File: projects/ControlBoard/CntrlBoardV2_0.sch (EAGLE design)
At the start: 106 parts

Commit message: Updated with processor test board V2
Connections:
- removed net PA12: SAMD21J.PA12
- net PA07: no longer C17.1, CH1-DM.A, CH2-DM.A, PH_AMP_2.OUT, R14.1, R34.2, TD-DM.1A
- net PB00: now also C17.1, CH1-DM.A, CH2-DM.A, PH_AMP_2.OUT, R14.1, R34.2, TD-DM.1A
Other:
- note added: "CONTAINS ERRORS IN PINNOUT DO NOT COPY"
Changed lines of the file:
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@@
 <?xml version="1.0" encoding="utf-8"?>
 <!DOCTYPE eagle SYSTEM "eagle.dtd">
-<eagle version="7.3.0">
+<eagle version="7.6.0">
 <drawing>
 <settings>
@@
 <text x="154.94" y="12.7" size="1.778" layer="95">Radio</text>
 <text x="152.4" y="86.36" size="1.778" layer="95">Solar Panels</text>
-<text x="152.4" y="96.52" size="1.778" layer="95">Sensors</text>
 <text x="152.4" y="104.14" size="1.778" layer="95">I2C</text>
 <text x="152.4" y="101.6" size="1.778" layer="95">I2C</text>
@@
 <text x="63.5" y="66.04" size="1.778" layer="95">NC</text>
 <text x="50.8" y="55.88" size="1.778" layer="97">RD_EN</text>
+<text x="187.96" y="91.44" size="1.778" layer="97">CONTAINS ERRORS IN PINNOUT DO NOT COPY</text>
 </plain>
 <instances>
@@
 </segment>
 </net>
-<net name="PA12" class="0">
-<segment>
-<pinref part="SAMD21J" gate="G$1" pin="PA12"/>
-<wire x1="149.86" y1="96.52" x2="139.7" y2="96.52" width="0.1524" layer="91"/>
-<label x="144.78" y="96.52" size="1.778" layer="95"/>
-</segment>
-</net>
 <net name="PA24" class="0">
 <segment>
@@
 </segment>
 </net>
-<net name="PA07" class="0">
+<net name="LFE_1_MP_NFLT" class="0">
+<segment>
+<pinref part="CH1-DM" gate="G$1" pin="B4"/>
+<wire x1="78.74" y1="88.9" x2="66.04" y2="88.9" width="0.1524" layer="91"/>
+<label x="58.42" y="88.9" size="1.778" layer="95"/>
+</segment>
+</net>
+<net name="VIN" class="0">
+<segment>
+<pinref part="CH2-DM" gate="G$1" pin="B5"/>
+<wire x1="180.34" y1="86.36" x2="193.04" y2="86.36" width="0.1524" layer="91"/>
+<label x="185.42" y="86.36" size="1.778" layer="95"/>
+</segment>
+</net>
+<net name="PB00" class="0">
 <segment>
 <pinref part="R14" gate="G$1" pin="1"/>
@@
 </segment>
 </net>
-<net name="LFE_1_MP_NFLT" class="0">
-<segment>
-<pinref part="CH1-DM" gate="G$1" pin="B4"/>
-<wire x1="78.74" y1="88.9" x2="66.04" y2="88.9" width="0.1524" layer="91"/>
-<label x="58.42" y="88.9" size="1.778" layer="95"/>
-</segment>
-</net>
-<net name="VIN" class="0">
-<segment>
-<pinref part="CH2-DM" gate="G$1" pin="B5"/>
-<wire x1="180.34" y1="86.36" x2="193.04" y2="86.36" width="0.1524" layer="91"/>
-<label x="185.42" y="86.36" size="1.778" layer="95"/>
-</segment>
-</net>

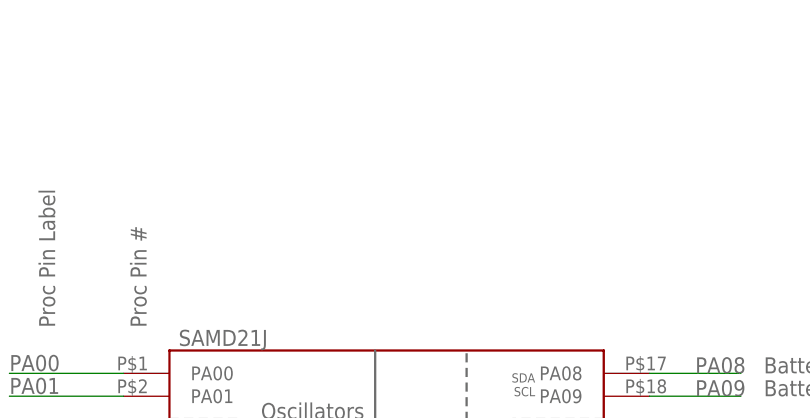
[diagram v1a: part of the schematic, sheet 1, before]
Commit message: LiFePO4 Balancing added
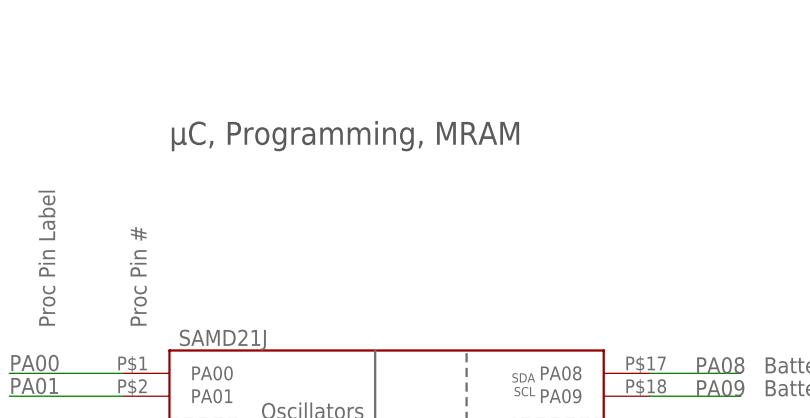
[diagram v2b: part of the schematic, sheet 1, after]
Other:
- note added: "Battery Board Buffers and Connector"
- note added: "Driver Board Connector"
- note added: "Radio Buffers, LEDs, and Connector"
- note added: "Signal Multiplexing"
- note added: "Solar Panel Connectors"
- note added: "Umbilical Connector"
- note added: "µC, Programming, MRAM"
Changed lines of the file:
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@@
 <?xml version="1.0" encoding="utf-8"?>
 <!DOCTYPE eagle SYSTEM "eagle.dtd">
-<eagle version="7.6.0">
+<eagle version="7.7.0">
 <drawing>
 <settings>
@@
 <text x="50.8" y="55.88" size="1.778" layer="97">RD_EN</text>
 <text x="187.96" y="91.44" size="1.778" layer="97">CONTAINS ERRORS IN PINNOUT DO NOT COPY</text>
+<text x="86.36" y="137.16" size="2.54" layer="97">µC, Programming, MRAM</text>
 </plain>
 <instances>
@@
 <plain>
 <text x="-2.54" y="119.38" size="1.27" layer="97">Note (PWM/SYNC) must have voltage greater than 1.5V to ensure PWM mode.</text>
+<text x="40.64" y="127" size="2.54" layer="97">Power Regulation</text>
 </plain>
 <instances>
@@
 <description>Sensors</description>
 <plain>
+<text x="30.48" y="71.12" size="2.54" layer="97">Sensors</text>
 </plain>
 <instances>
@@
 PB03 Return Enable
 PA25 Return In</text>
+<text x="-60.96" y="78.74" size="2.54" layer="97">Radio Buffers, LEDs, and Connector</text>
 </plain>
 <instances>
@@
 <description>Batteries</description>
 <plain>
+<text x="25.4" y="86.36" size="2.54" layer="97">Battery Board Buffers and Connector</text>
 </plain>
 <instances>
@@
 <plain>
 <text x="109.22" y="78.74" size="1.778" layer="97">IR_PMOS</text>
+<text x="35.56" y="101.6" size="2.54" layer="97">Solar Panel Connectors</text>
 </plain>
 <instances>
@@
 <wire x1="-17.78" y1="-15.24" x2="-17.78" y2="38.1" width="0.1524" layer="97" style="shortdash"/>
 <text x="-10.16" y="35.56" size="1.778" layer="97">Photodiode Conversion Circuit</text>
+<text x="-66.04" y="124.46" size="2.54" layer="97">Signal Multiplexing</text>
 </plain>
 <instances>
@@
 <text x="30.48" y="25.4" size="1.778" layer="97" rot="R270">Test Connection</text>
 <text x="121.92" y="76.2" size="1.778" layer="97">LED SHDN_N</text>
+<text x="12.7" y="96.52" size="2.54" layer="97">Driver Board Connector</text>
 </plain>
 <instances>
@@
 <text x="48.26" y="22.86" size="1.778" layer="97">Charging</text>
 <text x="48.26" y="17.78" size="1.778" layer="97">Umbilical Enable</text>
+<text x="-2.54" y="35.56" size="2.54" layer="97">Umbilical Connector</text>
 </plain>
 <instances>
